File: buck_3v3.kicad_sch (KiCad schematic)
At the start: 21 parts, among them U5 TPS564257DRLR

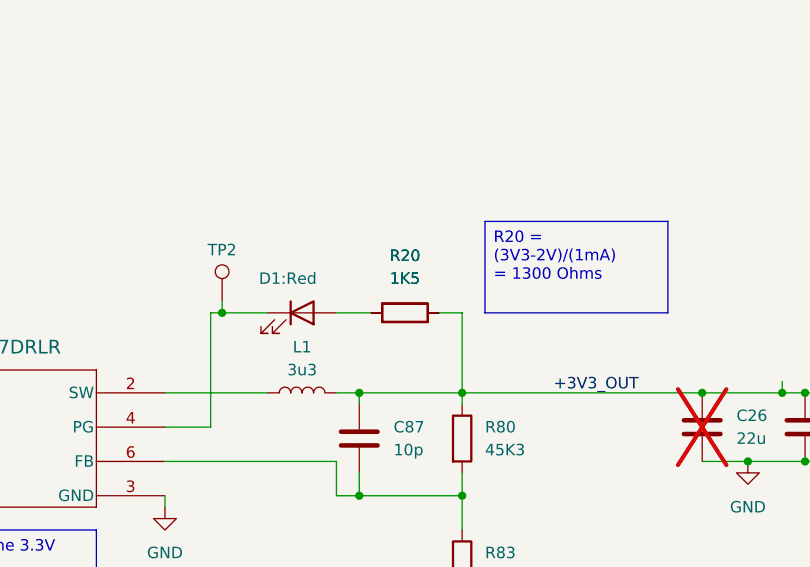
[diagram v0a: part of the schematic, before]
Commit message: towards a merge conflict free schematic. Refs: #9
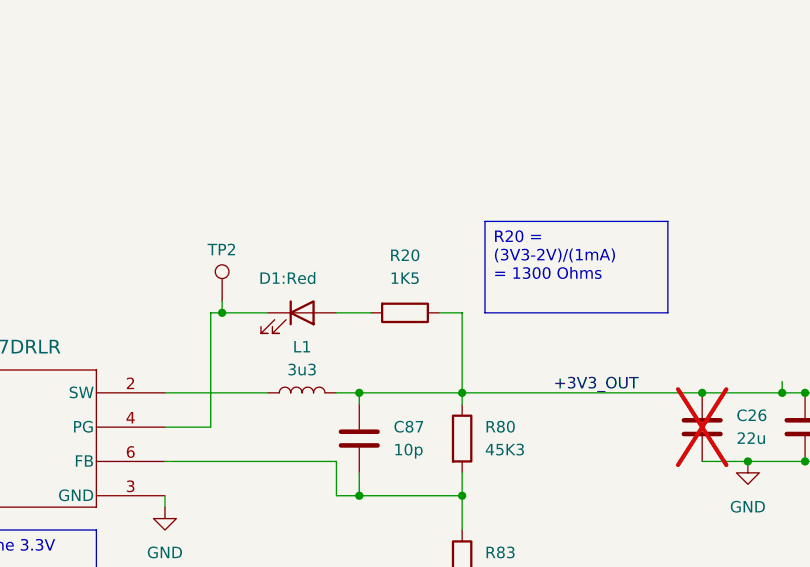
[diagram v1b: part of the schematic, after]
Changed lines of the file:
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@@
-	)
-	(symbol
-		(lib_id "KL_R:R_1K5_100mW_5_0603")
-		(at 173.99 63.5 270)
-		(unit 1)
-		(exclude_from_sim no)
-		(in_bom yes)
-		(on_board yes)
-		(dnp no)
-		(fields_autoplaced yes)
-		(property "Reference" "R20"
-			(at 173.99 57.15 90)
-			(effects
-				(font
-					(size 1.27 1.27)
-				)
-			)
-		)
-		(property "Value" "1K5"
-			(at 173.99 59.69 90)
-			(effects
-				(font
-					(size 1.27 1.27)
-				)
-			)
-		)
-		(property "Footprint" "KL_Footprints:R_0603"
-			(at 173.99 61.722 90)
-			(effects
-				(font
-					(size 1.27 1.27)
-				)
-				(hide yes)
-			)
-		)
-		(property "Datasheet" "https://yageogroup.com/content/Resource%20Library/Datasheet/PYU-AC_51_ROHS_L.pdf"
-			(at 173.99 63.5 0)
-			(effects
-				(font
-					(size 1.27 1.27)
-				)
-				(hide yes)
-			)
-		)
-		(property "Description" "Resistor"
-			(at 173.99 63.5 0)
-			(effects
-				(font
-					(size 1.27 1.27)
-				)
-				(hide yes)
-			)
-		)
-		(property "Power" "0.1"
-			(at 173.99 63.5 0)
-			(effects
-				(font
-					(size 1.27 1.27)
-				)
-				(hide yes)
-			)
-		)
-		(property "Tolerance" "5"
-			(at 173.99 63.5 0)
-			(effects
-				(font
-					(size 1.27 1.27)
-				)
-				(hide yes)
-			)
-		)
-		(property "Mouser" "603-AC0603JR-071K5L"
-			(at 173.99 63.5 0)
-			(effects
-				(font
-					(size 1.27 1.27)
-				)
-				(hide yes)
-			)
-		)
-		(property "Digikey" "YAG3645CT-ND"
-			(at 173.99 63.5 0)
-			(effects
-				(font
-					(size 1.27 1.27)
-				)
-				(hide yes)
-			)
-		)
-		(property "LCSC" "C49652951"
-			(at 173.99 63.5 0)
-			(effects
-				(font
-					(size 1.27 1.27)
-				)
-				(hide yes)
-			)
-		)
-		(property "Farnell" ""
-			(at 173.99 63.5 0)
-			(effects
-				(font
-					(size 1.27 1.27)
-				)
-				(hide yes)
-			)
-		)
-		(property "Package (in)" "0603"
-			(at 173.99 63.5 0)
-			(effects
-				(font
-					(size 1.27 1.27)
-				)
-				(hide yes)
-			)
-		)
-		(pin "1"
-		)
-		(pin "2"
-		)
-		(instances
-			(project ""
-				(path "/d4536448-b109-4159-96e2-3dc21baf2d6e/b46af5b7-dd4e-4356-ae8f-8ea1d81113b6"
-					(reference "R20")
-					(unit 1)
-				)
-			)
-		)
 	)
 	(symbol

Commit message: open project in KiCAD10. Refs: #41
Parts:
- TP16, TP17, TP18, TP2: value ~ -> (none)

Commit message: updates buck_3v3. Refs: #41
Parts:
- removed C74: 100n, KL_Footprints:C_0603, symbol KL_C:C_100n_10V_X7R_0603_10
- added C98: 100n, KL_Footprints:C_0603, symbol KL_C:C_100n_50V_10pct_X7R_0603
- C26, C73: symbol KL_C:C_22u_10V_X5R_0603_20 -> KL_C:C_22u_10V_20pct_X5R_0603; Dielectric (none) -> X5R; MPN (none) -> GRM187R61A226ME15D; Package_in_inch (none) -> 0603; Tolerance 20 -> (none); Tolerance_in_pct (none) -> 20; Voltage 10V -> (none); Voltage_in_V (none) -> 10
- C87: symbol KL_C:C_10p_25V_C0G_0603_5 -> KL_C:C_10p_25V_5pct_C0G_0603; Dielectric (none) -> C0G; MPN (none) -> 06033U100JAT2A; Package_in_inch (none) -> 0603; Tolerance 5 -> (none); Tolerance_in_pct (none) -> 5; Voltage 25V -> (none); Voltage_in_V (none) -> 25
- C88, C89: value 10uF -> 10u; symbol KL_C:C_10u_25V_X5R_0603_20 -> KL_C:C_10u_25V_20pct_X5R_0603; Dielectric (none) -> X5R; MPN (none) -> CL10A106MA8NRNC; Package_in_inch (none) -> 0603; Tolerance 20 -> (none); Tolerance_in_pct (none) -> 20; Voltage 25 -> (none); Voltage_in_V (none) -> 25
- C90: symbol KL_C:C_100n_16V_X7R_0603_10 -> KL_C:C_100n_16V_10pct_X7R_0603; Dielectric (none) -> X7R; MPN (none) -> CC0603KPX7R7BB104; Package_in_inch (none) -> 0603; Tolerance 10 -> (none); Tolerance_in_pct (none) -> 10; Voltage 16V -> (none); Voltage_in_V (none) -> 16
- C91: symbol KL_C:C_100n_50V_X7R_0603_10 -> KL_C:C_100n_50V_10pct_X7R_0603; Dielectric (none) -> X7R; MPN (none) -> CL10B104KB8NNNC; Package_in_inch (none) -> 0603; Tolerance 20 -> (none); Tolerance_in_pct (none) -> 10; Voltage 10 -> (none); Voltage_in_V (none) -> 50
- D1: symbol KL_LED:LED_red_2V_0.03A -> KL_LED:LED_Red_2V_0.03A_0603; MPN (none) -> LTST-C194KRKT; Package_in_inch (none) -> 0603
- L1: symbol KL_L:L_3u3_8A_20pct_7LX7W -> KL_L:L_3u3_8A_20pct_7.2x6.9; MPN (none) -> EXLA1V0603-3R3-R; Package_LxW_in_mm (none) -> 7.2x6.9; Package_in_mm L7XW7 -> (none)
- R125: symbol KL_R:R_20K_100mW_1_0603 -> KL_R:R_20K_0.1W_1pct_0603; MPN (none) -> RC0603FR-1320KL; Package (in) 0603 -> (none); Package_in_inch (none) -> 0603; Power 0.1 -> (none); Power_in_W (none) -> 0.1; Tolerance 1 -> (none); Tolerance_in_pct (none) -> 1
- R20: symbol KL_R:R_1K5_100mW_5_0603 -> KL_R:R_1K5_0.1W_5pct_0603; MPN (none) -> AC0603JR-071K5L; Package (in) 0603 -> (none); Package_in_inch (none) -> 0603; Power 0.1 -> (none); Power_in_W (none) -> 0.1; Tolerance 5 -> (none); Tolerance_in_pct (none) -> 5
- R23: symbol KL_R:R_0R_2W_5_2512 -> KL_R:R_0R_2W_5pct_2512; MPN (none) -> CRF2512-J/-000ELF; Mouser 652-CRF2512-J-000ELF -> 652-CRF2512-J-000ELF; Package (in) 2512 -> (none); Package_in_inch (none) -> 2512; Power 2 -> (none); Power_in_W (none) -> 2; Tolerance 5 -> (none); Tolerance_in_pct (none) -> 5
- R80: symbol KL_R:R_45K3_100mW_1_0603 -> KL_R:R_45K3_0.1W_1pct_0603; MPN (none) -> RC0603FR-0745K3L; Package (in) 0603 -> (none); Package_in_inch (none) -> 0603; Power 100 -> (none); Power_in_W (none) -> 0.1; Tolerance 1 -> (none); Tolerance_in_pct (none) -> 1
- R83: symbol KL_R:R_10K_100mW_1_0603 -> KL_R:R_10K_0.1W_1pct_0603; Farnell 2421850 -> (none); MPN (none) -> RC0603FR-0710KL; Package (in) 0603 -> (none); Package_in_inch (none) -> 0603; Power_in_W (none) -> 0.1; Tolerance_in_pct (none) -> 1
- R94: symbol KL_R:R_47K_100mW_1_0603 -> KL_R:R_47K_0.1W_1pct_0603; LCSC KTR03EZPF4702 -> C2090549; MPN (none) -> RC0603FR-0747KP; Package (in) 0603 -> (none); Package_in_inch (none) -> 0603; Power 0.1 -> (none); Power_in_W (none) -> 0.1; Tolerance 1 -> (none); Tolerance_in_pct (none) -> 1
- TP16, TP17, TP18, TP2: footprint Connector_PinHeader_2.54mm:PinHeader_1x01_P2.54mm_Vertical -> KL_Footprints:TestPoint; symbol KL_TP:TestPoint -> KL_TestPoint:TestPoint
- U5: MPN (none) -> TPS564257DRLR; VIN_MAX_V (none) -> 17; VIN_MIN_V (none) -> 3
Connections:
- net +3V3_OUT: now also C98.1
- net GND: now also C98.2

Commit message: updates 10pF capacitor. Refs: #41
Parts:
- C87: Digikey 06033U100JAT2A-ND -> 13-CC0603JRNPO8BN100CT-ND; LCSC C2229848 -> C1853175; MPN 06033U100JAT2A -> CC0603JRNPO8BN100; Mouser 581-06033U100JAT2A -> 603-CC0603JRNP8BN100
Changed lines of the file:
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@@
 			)
 		)
-		(property "Datasheet" "https://datasheets.kyocera-avx.com/U-Series.pdf"
+		(property "Datasheet" "https://yageogroup.com/download/specsheet/CC0603JRNPO8BN100"
 			(at 168.91 77.47 0)
 			(hide yes)
@@
 			)
 		)
-		(property "Mouser" "581-06033U100JAT2A"
+		(property "Mouser" "603-CC0603JRNP8BN100"
 			(at 168.91 77.47 0)
 			(hide yes)
@@
 			)
 		)
-		(property "Digikey" "06033U100JAT2A-ND"
+		(property "Digikey" "13-CC0603JRNPO8BN100CT-ND"
 			(at 168.91 77.47 0)
 			(hide yes)
@@
 			)
 		)
-		(property "LCSC" "C2229848"
+		(property "LCSC" "C1853175"
 			(at 168.91 77.47 0)
 			(hide yes)
@@
 			)
 		)
-		(property "MPN" "06033U100JAT2A"
+		(property "MPN" "CC0603JRNPO8BN100"
 			(at 168.91 77.47 0)
 			(hide yes)

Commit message: adds output jumper for +3V3. Refs: #49
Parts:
- removed R23: 0R, KL_Footprints:R_2512, symbol KL_R:R_0R_2W_5pct_2512
- added J15: Header_02x01_2.54mm_0mm_Straight, KL_Footprints:02x01_2.54mm_Header, symbol KL_Header:Header_02x01_2.54mm_0mm_Straight
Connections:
- net +3V3_OUT: now also J15.1 (Pin_1); no longer C87.1, L1.2, R20.1, R80.1
- net 5-12V: now also C88.1, C89.1, C90.1, R94.1, TP17.1, U5.1 (VIN)
- new net: C87.1, J15.2 (Pin_2), L1.2, R20.1, R80.1
